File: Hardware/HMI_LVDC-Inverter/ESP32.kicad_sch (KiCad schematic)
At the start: 40 parts, among them SW10 SW_MEC_5E, SW9 SW_MEC_5E, U3 ESP32-WROOM-32E, Y1 32.768KHz

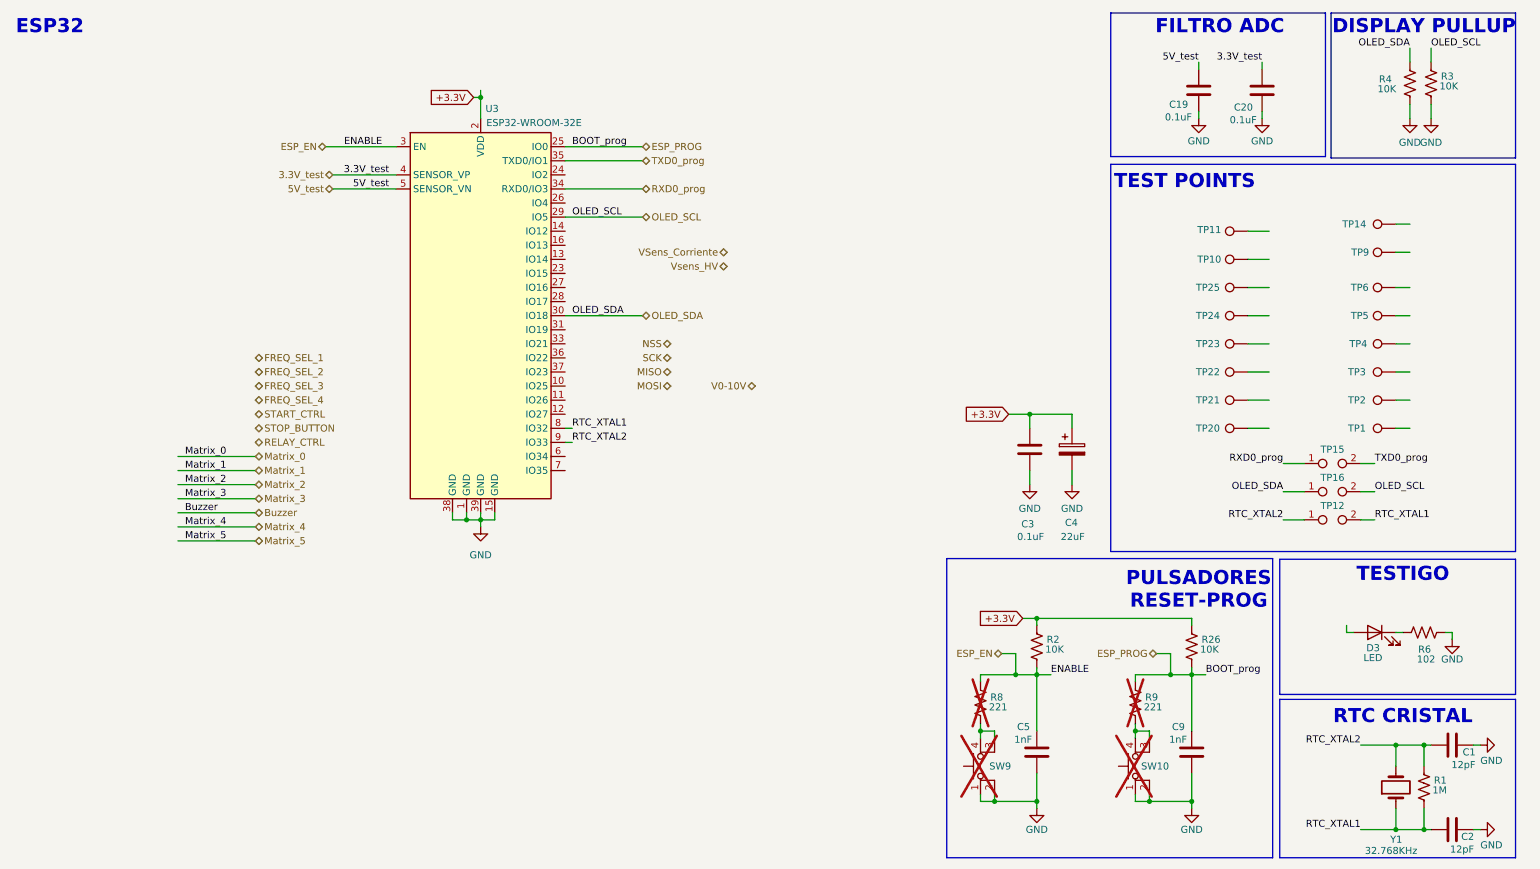
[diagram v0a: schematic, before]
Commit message: Terminado todo el conexionado eléctrico esquemático
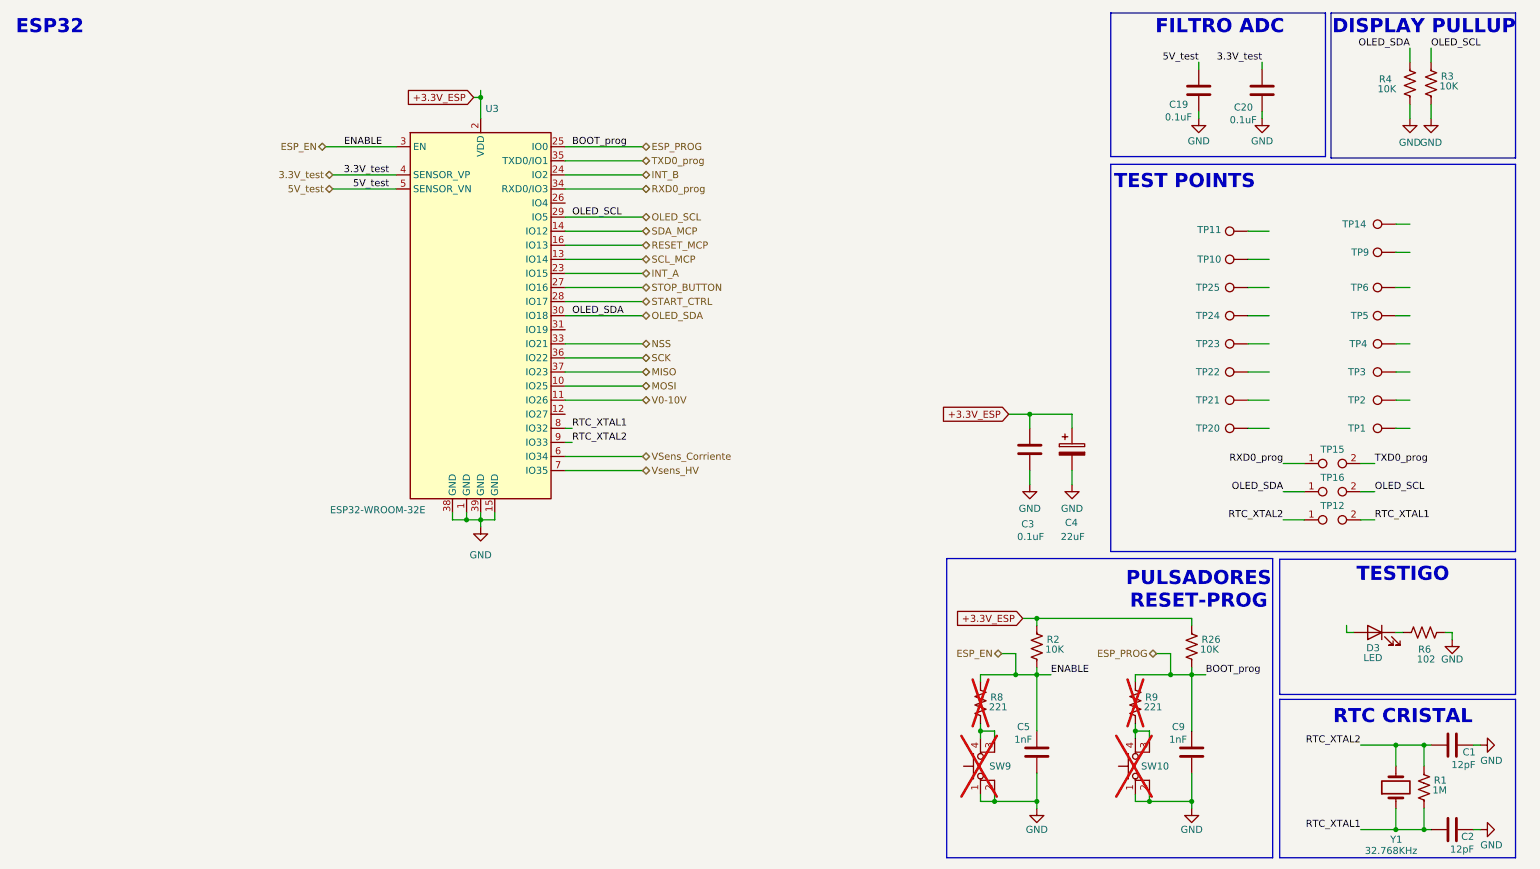
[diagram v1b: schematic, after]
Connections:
- net MISO: now also U3.37 (IO23)
- net MOSI: now also U3.10 (IO25)
- net NSS: now also U3.33 (IO21)
- net SCK: now also U3.36 (IO22)
- net START_CTRL: now also U3.28 (IO17)
- net STOP_BUTTON: now also U3.27 (IO16)
- net V0-10V: now also U3.11 (IO26)
- net VSens_Corriente: now also U3.6 (IO34)
- net Vsens_HV: now also U3.7 (IO35)
- net SCL_MCP: now reaches U3.13 (IO14)
- net SDA_MCP: now reaches U3.14 (IO12)
- net RESET_MCP: now reaches U3.16 (IO13)
- net INT_A: now reaches U3.23 (IO15)
- net INT_B: now reaches U3.24 (IO2)
- net +3.3V renamed +3.3V_ESP
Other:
- company: (none) -> Andrenacci - Carra
- title: (none) -> Variador de frecuencia LVDC

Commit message: Agregado de los componentes con links de compra en KiCAD a excepción de los conectores
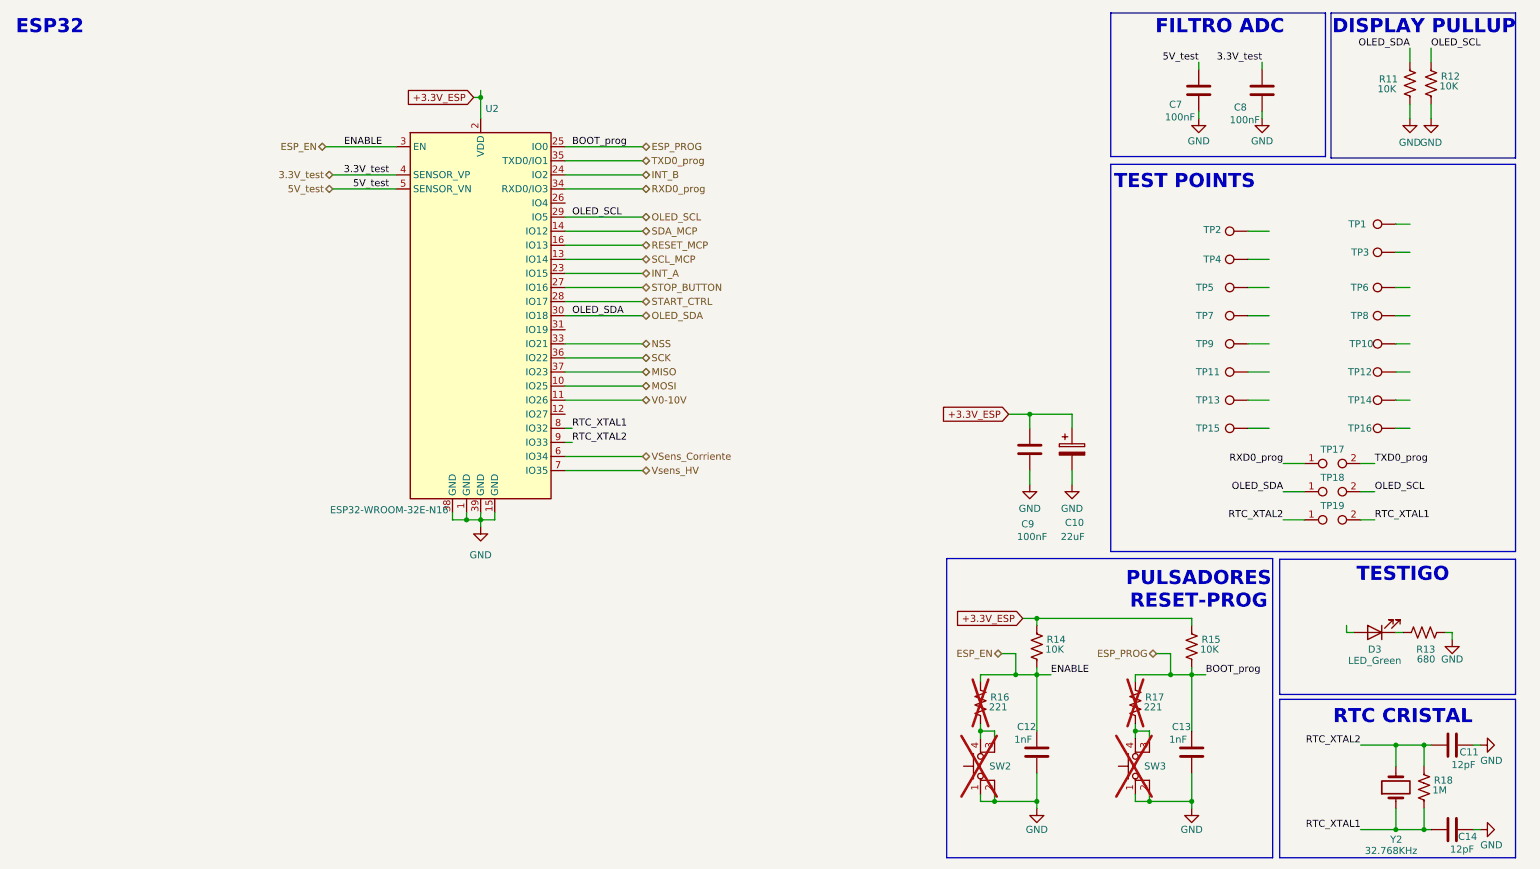
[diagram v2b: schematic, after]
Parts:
- C10: renamed from C4; footprint Capacitor_SMD:C_1206_3216Metric -> Capacitor_SMD:CP_Elec_5x5.4; Compra (none) -> https://www.lcsc.com/product-detail/C72502.html; Footprint checked (none) -> Yes; Manufacturer (none) -> Roquang; Price 0.6 -> 0.41; Symbol checked (none) -> Yes; currier https://ar.mouser.com/ProductDetail/TAIYO-YUDEN/EMK316BB722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 -> (none)
- C11: renamed from C1; Compra (none) -> https://www.lcsc.com/product-detail/C519482.html; Footprint checked (none) -> Yes; Manufacturer (none) -> Yagueo; Symbol checked (none) -> Yes; currier https://ar.mouser.com/ProductDetail/KYOCERA-AVX/06036C120KA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 -> (none)
- C12: renamed from C5; Compra (none) -> https://www.lcsc.com/product-detail/C100040.html?s_z=n_CC06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; Footprint checked (none) -> Yes; Manufacturer (none) -> Yagueo; Symbol checked (none) -> Yes; currier https://ar.mouser.com/ProductDetail/YAGEO/CC0603KRX7R7BB102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 -> (none)
- C13: renamed from C9; Compra (none) -> https://www.lcsc.com/product-detail/C100040.html?s_z=n_CC06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; Footprint checked (none) -> Yes; Manufacturer (none) -> Yagueo; Symbol checked (none) -> Yes; currier https://ar.mouser.com/ProductDetail/YAGEO/CC0603KRX7R7BB102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 -> (none)
- C14: renamed from C2; Compra (none) -> https://www.lcsc.com/product-detail/C519482.html; Footprint checked (none) -> Yes; Manufacturer (none) -> Yagueo; Symbol checked (none) -> Yes; currier https://ar.mouser.com/ProductDetail/KYOCERA-AVX/06036C120KA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 -> (none)
- C7: renamed from C19; value 0.1uF -> 100nF; footprint Capacitor_SMD:C_0603_1608Metric -> Capacitor_SMD:C_0603_1608Metric_Pad1.08x0.95mm_HandSolder; Compra (none) -> https://www.lcsc.com/product-detail/C14663.html; Footprint checked (none) -> Yes; Manufacturer (none) -> Yagueo; Price 0.1 -> 0.24; Symbol checked (none) -> Yes; currier https://ar.mouser.com/ProductDetail/YAGEO/CC0603KRX7R7BB104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 -> (none)
- C8: renamed from C20; value 0.1uF -> 100nF; footprint Capacitor_SMD:C_0603_1608Metric -> Capacitor_SMD:C_0603_1608Metric_Pad1.08x0.95mm_HandSolder; Compra (none) -> https://www.lcsc.com/product-detail/C14663.html; Footprint checked (none) -> Yes; Manufacturer (none) -> Yagueo; Price 0.1 -> 0.24; Symbol checked (none) -> Yes; currier https://ar.mouser.com/ProductDetail/YAGEO/CC0603KRX7R7BB104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 -> (none)
- C9: renamed from C3; value 0.1uF -> 100nF; footprint Capacitor_SMD:C_0603_1608Metric -> Capacitor_SMD:C_0603_1608Metric_Pad1.08x0.95mm_HandSolder; Compra (none) -> https://www.lcsc.com/product-detail/C14663.html; Footprint checked (none) -> Yes; Manufacturer (none) -> Yagueo; Price 0.1 -> 0.24; Symbol checked (none) -> Yes; currier https://ar.mouser.com/ProductDetail/YAGEO/CC0603KRX7R7BB104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 -> (none)
- D3: value LED -> LED_Green; footprint LED_SMD:LED_0805_2012Metric_Pad1.15x1.40mm_HandSolder -> LED_SMD:LED_0603_1608Metric_Pad1.05x0.95mm_HandSolder; Compra (none) -> https://www.lcsc.com/product-detail/C965804.html?s_z=n_XL-1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; Footprint checked (none) -> Yes; Manufacturer (none) -> XINGLIGHT; Price 0.31 -> 0.0044; Symbol checked (none) -> Yes; currier https://ar.mouser.com/ProductDetail/Dialight/599-0110-007F?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 -> (none)
- R11: renamed from R4; footprint (none) -> Resistor_SMD:R_0603_1608Metric_Pad0.98x0.95mm_HandSolder; Compra (none) -> https://www.lcsc.com/product-detail/C491211.html; Footprint checked (none) -> Yes; Manufacturer (none) -> PANASONIC; Price (none) -> 0.0321; Symbol checked (none) -> Yes
- R12: renamed from R3; footprint (none) -> Resistor_SMD:R_0603_1608Metric_Pad0.98x0.95mm_HandSolder; Compra (none) -> https://www.lcsc.com/product-detail/C491211.html; Footprint checked (none) -> Yes; Manufacturer (none) -> PANASONIC; Price (none) -> 0.0321; Symbol checked (none) -> Yes
- R13: renamed from R6; value 102 -> 680; footprint (none) -> Resistor_SMD:R_0603_1608Metric_Pad0.98x0.95mm_HandSolder; Compra (none) -> https://www.lcsc.com/product-detail/C20109434.html; Footprint checked (none) -> Yes; Manufacturer (none) -> ROHM; Price (none) -> 0.0186; Symbol checked (none) -> Yes
- R14: renamed from R2; footprint (none) -> Resistor_SMD:R_0603_1608Metric_Pad0.98x0.95mm_HandSolder; Compra (none) -> https://www.lcsc.com/product-detail/C491211.html; Footprint checked (none) -> Yes; Manufacturer (none) -> PANASONIC; Price (none) -> 0.0321; Symbol checked (none) -> Yes
- R15: renamed from R26; footprint (none) -> Resistor_SMD:R_0603_1608Metric_Pad0.98x0.95mm_HandSolder; Compra (none) -> https://www.lcsc.com/product-detail/C491211.html; Footprint checked (none) -> Yes; Manufacturer (none) -> PANASONIC; Price (none) -> 0.0321; Symbol checked (none) -> Yes
- R18: renamed from R1; footprint (none) -> Resistor_SMD:R_0603_1608Metric_Pad0.98x0.95mm_HandSolder; Compra (none) -> https://www.lcsc.com/product-detail/C2074499.html; Footprint checked (none) -> Yes; Manufacturer (none) -> VISHAY; Price (none) -> 0.0357; Symbol checked (none) -> Yes
- SW2: renamed from SW9; Manufacturer (none) -> https://ar.mouser.com/ProductDetail/Same-Sky/TS34-62-35-BK-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; currier https://ar.mouser.com/ProductDetail/Same-Sky/TS34-62-35-BK-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 -> (none)
- SW3: renamed from SW10; Manufacturer (none) -> https://ar.mouser.com/ProductDetail/Same-Sky/TS34-62-35-BK-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; currier https://ar.mouser.com/ProductDetail/Same-Sky/TS34-62-35-BK-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 -> (none)
- U2: renamed from U3; value ESP32-WROOM-32E -> ESP32-WROOM-32E-N16; Compra (none) -> https://www.lcsc.com/product-detail/C701343.html?s_z=n_ESP3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; Manufacturer (none) -> ESPRESSIF; Price 6.71 -> 4.9252; currier https://ar.mouser.com/ProductDetail/Espressif-Systems/ESP32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 -> (none)
- Y2: renamed from Y1; footprint (none) -> Crystal:Crystal_SMD_3215-2Pin_3.2x1.5mm; Compra (none) -> https://www.lcsc.com/product-detail/C32346.html; Footprint checked (none) -> Yes; Manufacturer (none) -> EPSON; Price 0.53 -> 0.1898; Symbol checked (none) -> Yes; currier https://ar.mouser.com/ProductDetail/70-XT1312HHRXX32K76E -> (none)
- renumbered R8 to R16, R9 to R17, TP14 to TP1, TP4 to TP10, TP22 to TP11, TP3 to TP12, TP21 to TP13, TP2 to TP14, TP20 to TP15, TP1 to TP16, TP15 to TP17, TP16 to TP18, TP12 to TP19, TP11 to TP2, TP9 to TP3, TP10 to TP4, TP25 to TP5, TP24 to TP7, TP5 to TP8, TP23 to TP9

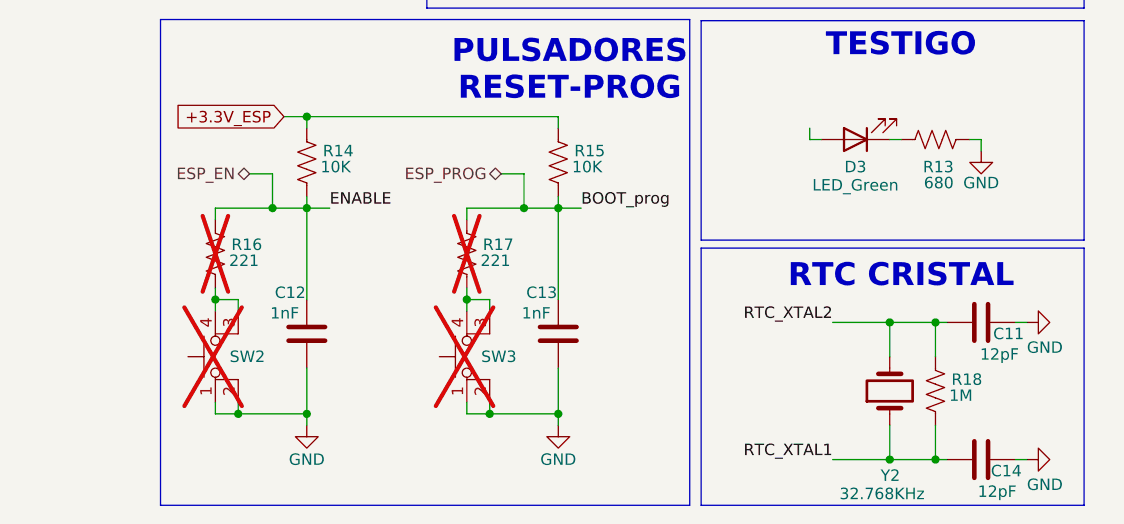
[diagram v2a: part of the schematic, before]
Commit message: Avances en el PCB, arreglos en el esquema y agregado de borneras de gabinete
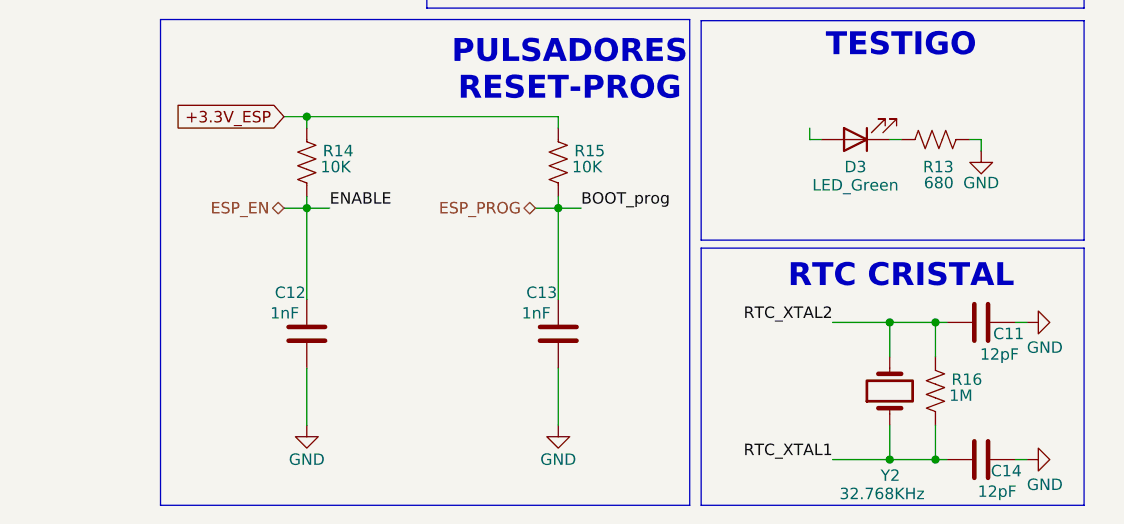
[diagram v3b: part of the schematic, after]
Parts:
- removed R16, R17: 221, symbol Device:R_US
- removed SW2, SW3: SW_MEC_5E, Button_Switch_SMD:SW_MEC_5GSH9, symbol Switch:SW_MEC_5E
- renumbered R18 to R16
